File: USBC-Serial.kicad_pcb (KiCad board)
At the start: 2 copper layers, 19.5 x 29.2 mm, 10 parts, among them J1 USB_C_Receptacle_USB2.0_16P, J2 Conn_01x06_Pin, U1 CH343P

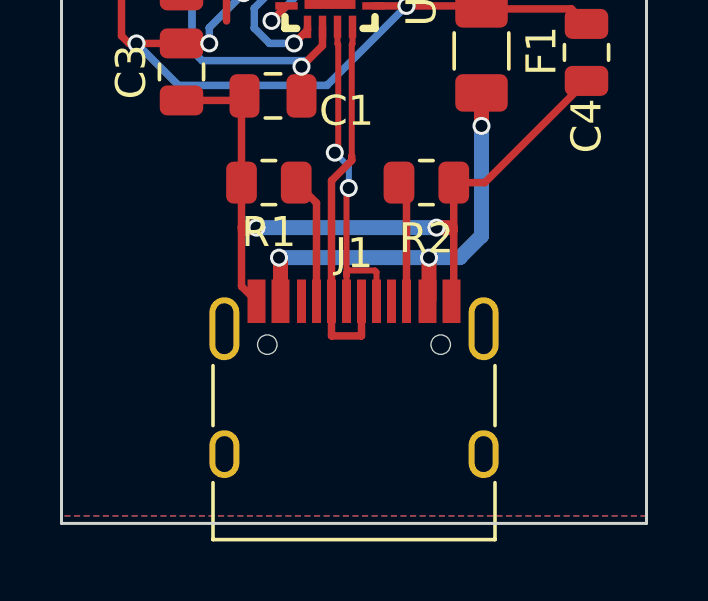
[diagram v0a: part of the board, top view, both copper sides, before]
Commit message: add Type-C GND to shell connection
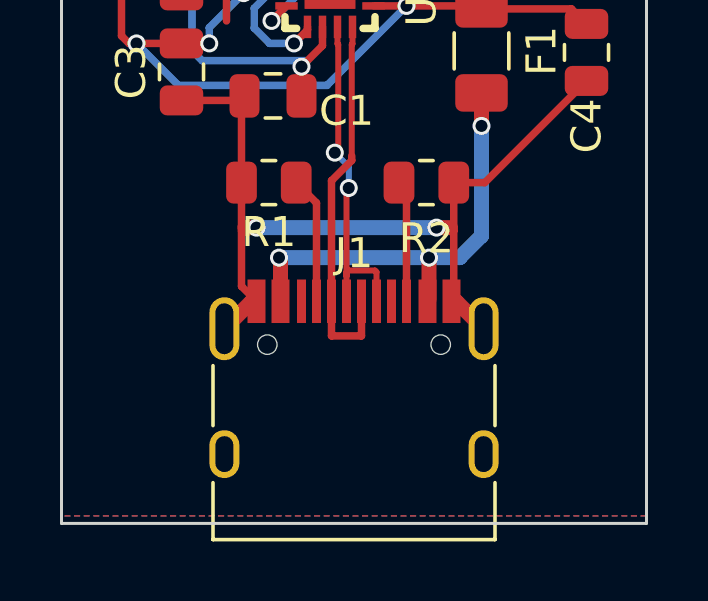
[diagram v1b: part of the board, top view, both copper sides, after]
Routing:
- net GND: track 33.9 -> 36.8 mm
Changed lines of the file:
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@@
   (segment (start 19 28.1) (end 19.1 28) (width 0.25) (layer "F.Cu") (net 2))
   (segment (start 20.5 24) (end 18.5 24) (width 0.25) (layer "F.Cu") (net 2))
+  (segment (start 26.155 34.845483) (end 27.07 35.760483) (width 0.5) (layer "F.Cu") (net 2))
   (segment (start 26.075 32.5) (end 26.075 34.770483) (width 0.25) (layer "F.Cu") (net 2))
   (segment (start 18.5 24) (end 18.25 24) (width 0.25) (layer "F.Cu") (net 2))
+  (segment (start 26 34.845483) (end 26.155 34.845483) (width 0.5) (layer "F.Cu") (net 2))
   (segment (start 26.075 30.890483) (end 27.109517 30.890483) (width 0.25) (layer "F.Cu") (net 2))
+  (segment (start 19.5 34.845483) (end 19.345 34.845483) (width 0.5) (layer "F.Cu") (net 2))
   (segment (start 21.95 24.25) (end 21.7 24.5) (width 0.25) (layer "F.Cu") (net 2))
   (segment (start 19 34.345483) (end 19.5 34.845483) (width 0.25) (layer "F.Cu") (net 2))
@@
   (segment (start 25.5 32.390483) (end 25.965483 32.390483) (width 0.5) (layer "F.Cu") (net 2))
   (segment (start 19 32.5) (end 19 34.345483) (width 0.25) (layer "F.Cu") (net 2))
+  (segment (start 19.345 34.845483) (end 18.43 35.760483) (width 0.5) (layer "F.Cu") (net 2))
   (segment (start 21.7 24) (end 20.5 24) (width 0.25) (layer "F.Cu") (net 2))
   (segment (start 18.5 24) (end 18.5 25.5) (width 0.25) (layer "F.Cu") (net 2))

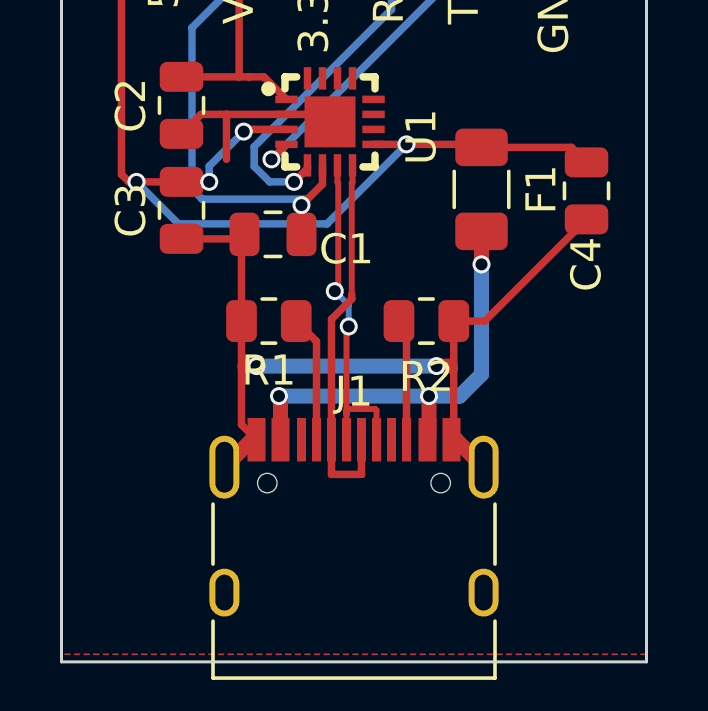
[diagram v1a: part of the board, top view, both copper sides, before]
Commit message: Redo D+ D- track, reroute R1 R2
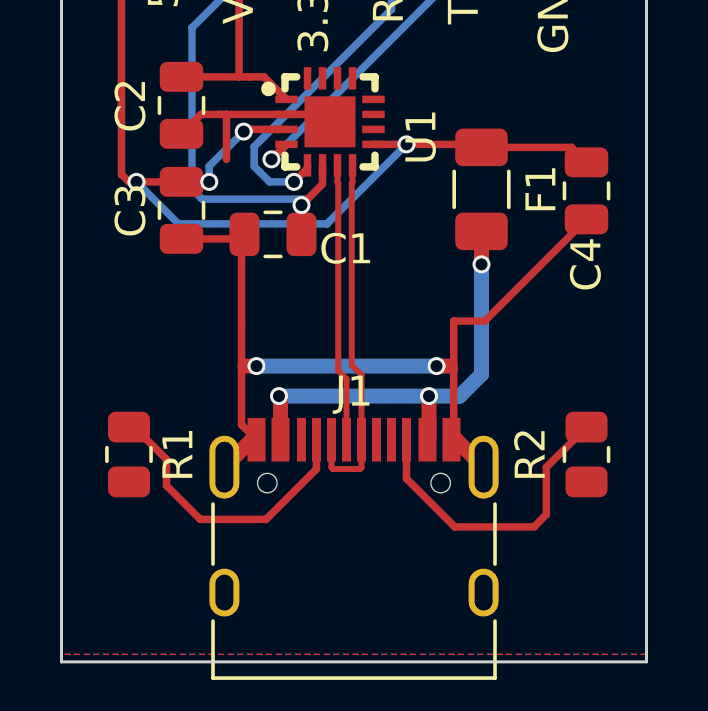
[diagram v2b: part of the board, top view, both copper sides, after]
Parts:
- moved R2 6.95 mm to (30.5, 35.3), turned to -90 degrees
- moved R1 6.44 mm to (15.2, 35.3), turned to -90 degrees
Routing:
- net Net-(J1-CC2): track 4.06 -> 10.3 mm
- net Net-(J1-CC1): track 4.23 -> 9.71 mm
- net /D+: track 11.6 -> 9.27 mm, vias 2 -> 0
- net /D-: track 12.7 -> 12.2 mm
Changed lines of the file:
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@@
   )
   (footprint "Resistor_SMD:R_0805_2012Metric" (layer "F.Cu")
-    (at 19.9125 30.890483 180)
+    (at 15.25 35.3375 -90)
     (descr "Resistor SMD 0805 (2012 Metric), square (rectangular) end terminal, IPC_7351 nominal, (Body size source: IPC-SM-782 page 72, https://www.pcb-3d.com/wordpress/wp-content/uploads/ipc-sm-782a_amendment_1_and_2.pdf), generated with kicad-footprint-generator")
     (tags "resistor")
@@
     (property "ki_keywords" "R res resistor")
     (attr smd)
-    (fp_text reference "R1" (at 0 -1.65) (layer "F.SilkS")
-        (effects (font (size 1 1) (thickness 0.15)))
-    )
-    (fp_text value "5.1k" (at 0.1625 1.75) (layer "F.Fab") hide
-        (effects (font (size 1 1) (thickness 0.15)))
-    )
-    (fp_text user "${REFERENCE}" (at 0 0) (layer "F.Fab")
+    (fp_text reference "R1" (at 0 -1.65 -270) (layer "F.SilkS")
+        (effects (font (size 1 1) (thickness 0.15)))
+    )
+    (fp_text value "5.1k" (at 0.1625 1.75 -270) (layer "F.Fab") hide
+        (effects (font (size 1 1) (thickness 0.15)))
+    )
+    (fp_text user "${REFERENCE}" (at 0 0 -270) (layer "F.Fab")
         (effects (font (size 0.5 0.5) (thickness 0.08)))
     )
@@
     (fp_line (start 1 0.625) (end -1 0.625)
       (stroke (width 0.1) (type solid)) (layer "F.Fab"))
-    (pad "1" smd roundrect (at -0.9125 0 180) (size 1.025 1.4) (layers "F.Cu" "F.Paste" "F.Mask") (roundrect_rratio 0.243902439)
+    (pad "1" smd roundrect (at -0.9125 0 270) (size 1.025 1.4) (layers "F.Cu" "F.Paste" "F.Mask") (roundrect_rratio 0.243902439)
       (net 6 "Net-(J1-CC1)") (pintype "passive"))
-    (pad "2" smd roundrect (at 0.9125 0 180) (size 1.025 1.4) (layers "F.Cu" "F.Paste" "F.Mask") (roundrect_rratio 0.243902439)
+    (pad "2" smd roundrect (at 0.9125 0 270) (size 1.025 1.4) (layers "F.Cu" "F.Paste" "F.Mask") (roundrect_rratio 0.243902439)
       (net 2 "GND") (pintype "passive"))
     (model "${KICAD6_3DMODEL_DIR}/Resistor_SMD.3dshapes/R_0805_2012Metric.wrl"
@@
   )
   (footprint "Resistor_SMD:R_0805_2012Metric" (layer "F.Cu")
-    (at 25.1625 30.890483)
+    (at 30.5 35.3375 -90)
     (descr "Resistor SMD 0805 (2012 Metric), square (rectangular) end terminal, IPC_7351 nominal, (Body size source: IPC-SM-782 page 72, https://www.pcb-3d.com/wordpress/wp-content/uploads/ipc-sm-782a_amendment_1_and_2.pdf), generated with kicad-footprint-generator")
     (tags "resistor")
@@
     (property "ki_keywords" "R res resistor")
     (attr smd)
-    (fp_text reference "R2" (at 0 1.859517) (layer "F.SilkS")
-        (effects (font (size 1 1) (thickness 0.15)))
-    )
-    (fp_text value "5.1k" (at 0 1.65) (layer "F.Fab") hide
-        (effects (font (size 1 1) (thickness 0.15)))
-    )
-    (fp_text user "${REFERENCE}" (at 0 0) (layer "F.Fab")
+    (fp_text reference "R2" (at 0 1.859517 90) (layer "F.SilkS")
+        (effects (font (size 1 1) (thickness 0.15)))
+    )
+    (fp_text value "5.1k" (at 0 1.65 90) (layer "F.Fab") hide
+        (effects (font (size 1 1) (thickness 0.15)))
+    )
+    (fp_text user "${REFERENCE}" (at 0 0 90) (layer "F.Fab")
         (effects (font (size 0.5 0.5) (thickness 0.08)))
     )
@@
     (fp_line (start 1 0.625) (end -1 0.625)
       (stroke (width 0.1) (type solid)) (layer "F.Fab"))
-    (pad "1" smd roundrect (at -0.9125 0) (size 1.025 1.4) (layers "F.Cu" "F.Paste" "F.Mask") (roundrect_rratio 0.243902439)
+    (pad "1" smd roundrect (at -0.9125 0 270) (size 1.025 1.4) (layers "F.Cu" "F.Paste" "F.Mask") (roundrect_rratio 0.243902439)
       (net 10 "Net-(J1-CC2)") (pintype "passive"))
-    (pad "2" smd roundrect (at 0.9125 0) (size 1.025 1.4) (layers "F.Cu" "F.Paste" "F.Mask") (roundrect_rratio 0.243902439)
+    (pad "2" smd roundrect (at 0.9125 0 270) (size 1.025 1.4) (layers "F.Cu" "F.Paste" "F.Mask") (roundrect_rratio 0.243902439)
       (net 2 "GND") (pintype "passive"))
     (model "${KICAD6_3DMODEL_DIR}/Resistor_SMD.3dshapes/R_0805_2012Metric.wrl"
@@
   (segment (start 20.25 33.390483) (end 25.25 33.390483) (width 0.5) (layer "B.Cu") (net 5))
   (segment (start 26.277082 33.390483) (end 27 32.667565) (width 0.5) (layer "B.Cu") (net 5))
-  (segment (start 20.825 30.890483) (end 21.5 31.565483) (width 0.25) (layer "F.Cu") (net 6))
-  (segment (start 21.5 31.565483) (end 21.5 34.845483) (width 0.25) (layer "F.Cu") (net 6))
-  (segment (start 22.55 33.820483) (end 23.45 33.820483) (width 0.2) (layer "F.Cu") (net 7))
+  (segment (start 17.625 37.5) (end 16.5 36.375) (width 0.25) (layer "F.Cu") (net 6))
+  (segment (start 15.425 34.425) (end 15.25 34.425) (width 0.25) (layer "F.Cu") (net 6))
+  (segment (start 21.5 35.820483) (end 19.820483 37.5) (width 0.25) (layer "F.Cu") (net 6))
+  (segment (start 16.5 35.5) (end 15.425 34.425) (width 0.25) (layer "F.Cu") (net 6))
+  (segment (start 19.820483 37.5) (end 17.625 37.5) (width 0.25) (layer "F.Cu") (net 6))
+  (segment (start 16.5 36.375) (end 16.5 35.5) (width 0.25) (layer "F.Cu") (net 6))
+  (segment (start 21.5 34.845483) (end 21.5 35.820483) (width 0.25) (layer "F.Cu") (net 6))
+  (segment (start 22.225 32.5432) (end 22.5 32.8182) (width 0.2) (layer "F.Cu") (net 7))
+  (segment (start 22.225 26.287501) (end 22.225 32.5432) (width 0.2) (layer "F.Cu") (net 7))
+  (segment (start 22.5 32.8182) (end 22.5 34.845483) (width 0.2) (layer "F.Cu") (net 7))
   (segment (start 22.2 25.7) (end 22.2 26.262501) (width 0.2) (layer "F.Cu") (net 7))
-  (segment (start 22.5 33.870483) (end 22.55 33.820483) (width 0.2) (layer "F.Cu") (net 7))
-  (segment (start 22.5 34) (end 22.5 31.144608) (width 0.2) (layer "F.Cu") (net 7))
-  (segment (start 23.45 33.820483) (end 23.5 33.870483) (width 0.2) (layer "F.Cu") (net 7))
-  (segment (start 23.5 33.870483) (end 23.5 34.845483) (width 0.2) (layer "F.Cu") (net 7))
-  (segment (start 22.5 34) (end 22.5 33.870483) (width 0.2) (layer "F.Cu") (net 7))
-  (segment (start 22.225 26.287501) (end 22.225 30) (width 0.2) (layer "F.Cu") (net 7))
-  (segment (start 22.5 31.144608) (end 22.575 31.069608) (width 0.2) (layer "F.Cu") (net 7))
-  (segment (start 22.5 34.845483) (end 22.5 34) (width 0.2) (layer "F.Cu") (net 7))
   (segment (start 22.2 26.262501) (end 22.225 26.287501) (width 0.2) (layer "F.Cu") (net 7))
-  (via (at 22.575 31.069608) (size 0.6) (drill 0.4) (layers "F.Cu" "B.Cu") (net 7))
-  (via (at 22.110183 29.892265) (size 0.6) (drill 0.4) (layers "F.Cu" "B.Cu") (net 7))
-  (segment (start 22.575 31.069608) (end 22.575 30.357082) (width 0.2) (layer "B.Cu") (net 7))
-  (segment (start 22.575 30.357082) (end 22.110183 29.892265) (width 0.2) (layer "B.Cu") (net 7))
-  (segment (start 22 36) (end 22 34.845483) (width 0.25) (layer "F.Cu") (net 8))
-  (segment (start 22 30.826041) (end 22.675 30.151041) (width 0.25) (layer "F.Cu") (net 8))
-  (segment (start 22 36) (end 23 36) (width 0.25) (layer "F.Cu") (net 8))
-  (segment (start 22.675 26.287501) (end 22.675 30) (width 0.2) (layer "F.Cu") (net 8))
-  (segment (start 23 34.845483) (end 23 36) (width 0.25) (layer "F.Cu") (net 8))
+  (segment (start 22 34.845483) (end 22 35.770483) (width 0.2) (layer "F.Cu") (net 8))
+  (segment (start 23 32.6818) (end 23 34.845483) (width 0.2) (layer "F.Cu") (net 8))
+  (segment (start 22.675 32.3568) (end 23 32.6818) (width 0.2) (layer "F.Cu") (net 8))
+  (segment (start 22.05 35.820483) (end 22.95 35.820483) (width 0.2) (layer "F.Cu") (net 8))
+  (segment (start 22.95 35.820483) (end 23 35.770483) (width 0.2) (layer "F.Cu") (net 8))
+  (segment (start 23 35.770483) (end 23 34.845483) (width 0.2) (layer "F.Cu") (net 8))
   (segment (start 22.7 26.262501) (end 22.675 26.287501) (width 0.2) (layer "F.Cu") (net 8))
-  (segment (start 22 34.845483) (end 22 30.826041) (width 0.25) (layer "F.Cu") (net 8))
+  (segment (start 22 35.770483) (end 22.05 35.820483) (width 0.2) (layer "F.Cu") (net 8))
   (segment (start 22.7 25.7) (end 22.7 26.262501) (width 0.2) (layer "F.Cu") (net 8))
-  (segment (start 22.675 30.151041) (end 22.675 30) (width 0.25) (layer "F.Cu") (net 8))
-  (segment (start 24.5 31.140483) (end 24.5 34.845483) (width 0.25) (layer "F.Cu") (net 10))
-  (segment (start 24.25 30.890483) (end 24.5 31.140483) (width 0.25) (layer "F.Cu") (net 10))
+  (segment (start 22.675 26.287501) (end 22.675 32.3568) (width 0.2) (layer "F.Cu") (net 8))
+  (segment (start 29.16189 35.76311) (end 30.5 34.425) (width 0.25) (layer "F.Cu") (net 10))
+  (segment (start 24.5 36.140432) (end 26.109568 37.75) (width 0.25) (layer "F.Cu") (net 10))
+  (segment (start 26.109568 37.75) (end 28.75 37.75) (width 0.25) (layer "F.Cu") (net 10))
+  (segment (start 29.16189 37.33811) (end 29.16189 35.76311) (width 0.25) (layer "F.Cu") (net 10))
+  (segment (start 24.5 34.845483) (end 24.5 36.140432) (width 0.25) (layer "F.Cu") (net 10))
+  (segment (start 28.75 37.75) (end 29.16189 37.33811) (width 0.25) (layer "F.Cu") (net 10))
   (segment (start 21.2 25.7) (end 21.2 25.8) (width 0.25) (layer "F.Cu") (net 12))
   (segment (start 21.2 25.8) (end 20.75 26.25) (width 0.25) (layer "F.Cu") (net 12))

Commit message: nuke everything - major refactor
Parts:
- moved C2 19.2 mm to (36.2, 24.9), turned to 0 degrees
- moved C3 19.2 mm to (36.2, 28.0), turned to 0 degrees
- moved U1 18.9 mm to (40.8, 26.1), turned to 0 degrees
- moved C1 17.2 mm to (36.2, 21.9), turned to 0 degrees
- moved F1 14.9 mm to (41.2, 22.1), turned to 0 degrees
- moved C4 7.21 mm to (36.2, 31.0), turned to 0 degrees
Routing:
- net +5V: track 34.2 -> 0.00 mm, vias 4 -> 0
- net GND: track 36.8 -> 3.71 mm, vias 2 -> 0
- net +3.3V: track 18.1 -> 0.00 mm, vias 1 -> 0
- net /TXD: track 11.9 -> 0.00 mm, vias 1 -> 0
- net /RXD: track 12.9 -> 1.35 mm, vias 1 -> 0
- net /VIO: track 9.56 -> 0.00 mm
- net /D-: track 12.2 -> 2.89 mm
- net /D+: track 9.27 -> 0.00 mm
- net /VBUS: track 14.8 -> 7.95 mm, vias 3 -> 0
- net Net-(J1-CC2): track 10.3 -> 9.47 mm
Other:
- board text removed: "3.3V"
- board text removed: "5V"
- board text removed: "GND"
- board text removed: "RX"
- board text removed: "TX"
- board text removed: "VIO"

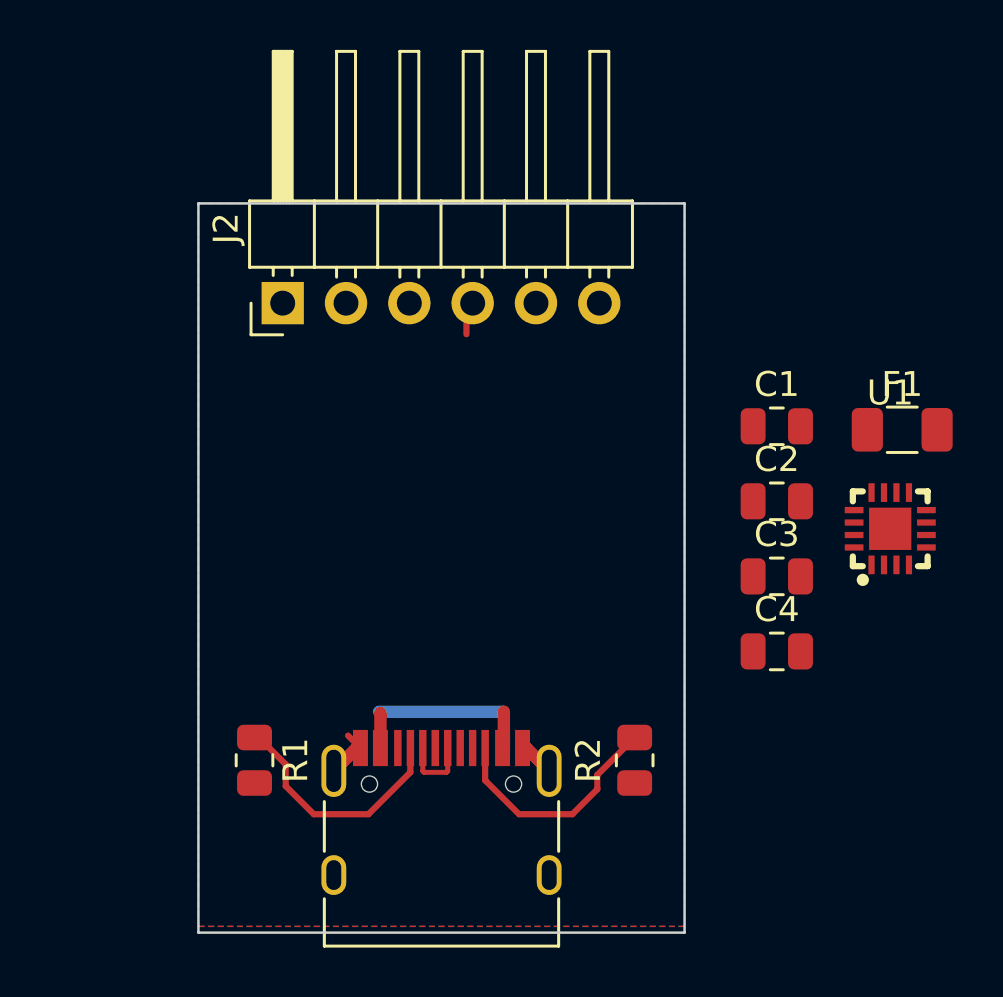
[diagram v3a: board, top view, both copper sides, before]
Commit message: refactor, rotated the main chip for 90 degrees
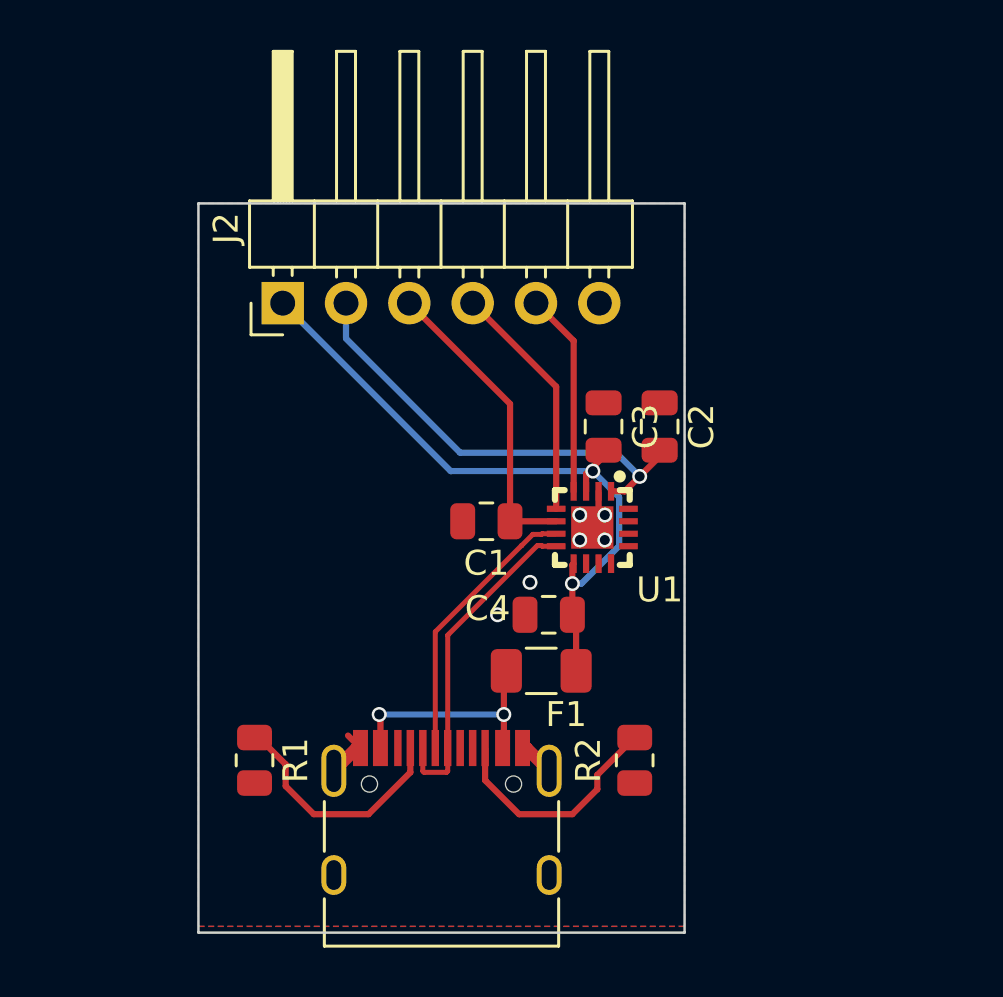
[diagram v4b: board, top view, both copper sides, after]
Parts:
- moved F1 17.4 mm to (26.8, 31.8)
- moved C1 12.3 mm to (24.6, 25.8), turned to 180 degrees
- moved U1 12.0 mm to (28.8, 26.0), turned to 180 degrees
- moved C4 9.27 mm to (27.1, 29.5), turned to 180 degrees
- moved C3 9.19 mm to (29.2, 21.9), turned to -90 degrees
- moved C2 5.58 mm to (31.5, 21.9), turned to -90 degrees
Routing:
- net +5V: track 0.00 -> 27.6 mm, vias 0 -> 2
- net /VIO: track 0.00 -> 18.0 mm, vias 0 -> 1
- net +3.3V: track 0.00 -> 12.3 mm
- net /D+: track 0.00 -> 11.1 mm
- net /D-: track 2.89 -> 13.3 mm
- net /RXD: track 1.35 -> 9.99 mm
- net /TXD: track 0.00 -> 8.18 mm
- net GND: track 3.71 -> 5.62 mm, vias 0 -> 6
- net /VBUS: track 7.95 -> 9.52 mm, vias 0 -> 2
